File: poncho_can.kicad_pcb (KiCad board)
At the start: 2 copper layers, 85.7 x 79.6 mm, 40 parts, among them J10 GS2, J101 DB9_Male_MountingHoles, J102 DB9_Male_MountingHoles, J103 GS2, J104 GS2, J105 GS2, J106 GS2, J7 GS2, J8 GS2, J9 GS2, U101 TJA1051T, U102 TJA1051T

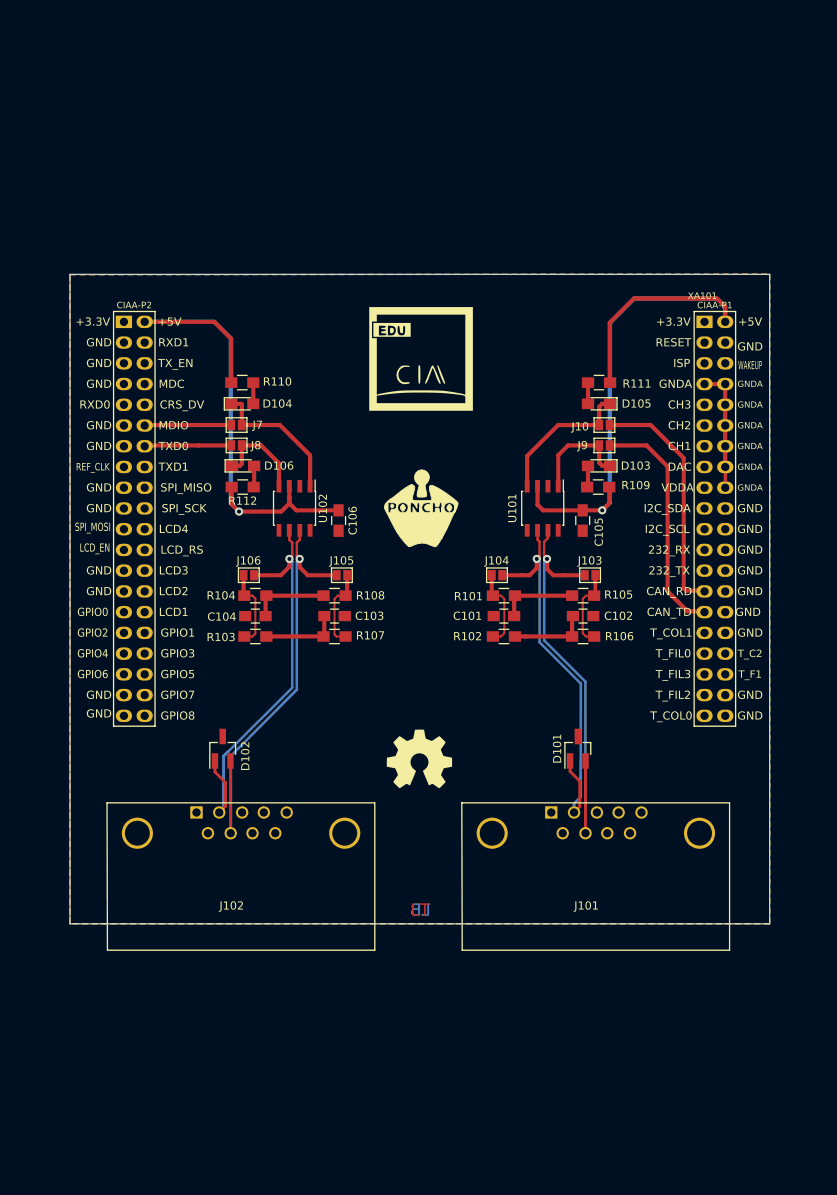
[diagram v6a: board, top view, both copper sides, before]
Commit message: Agrego documentacion y aplica cambios sugeridos en la revision
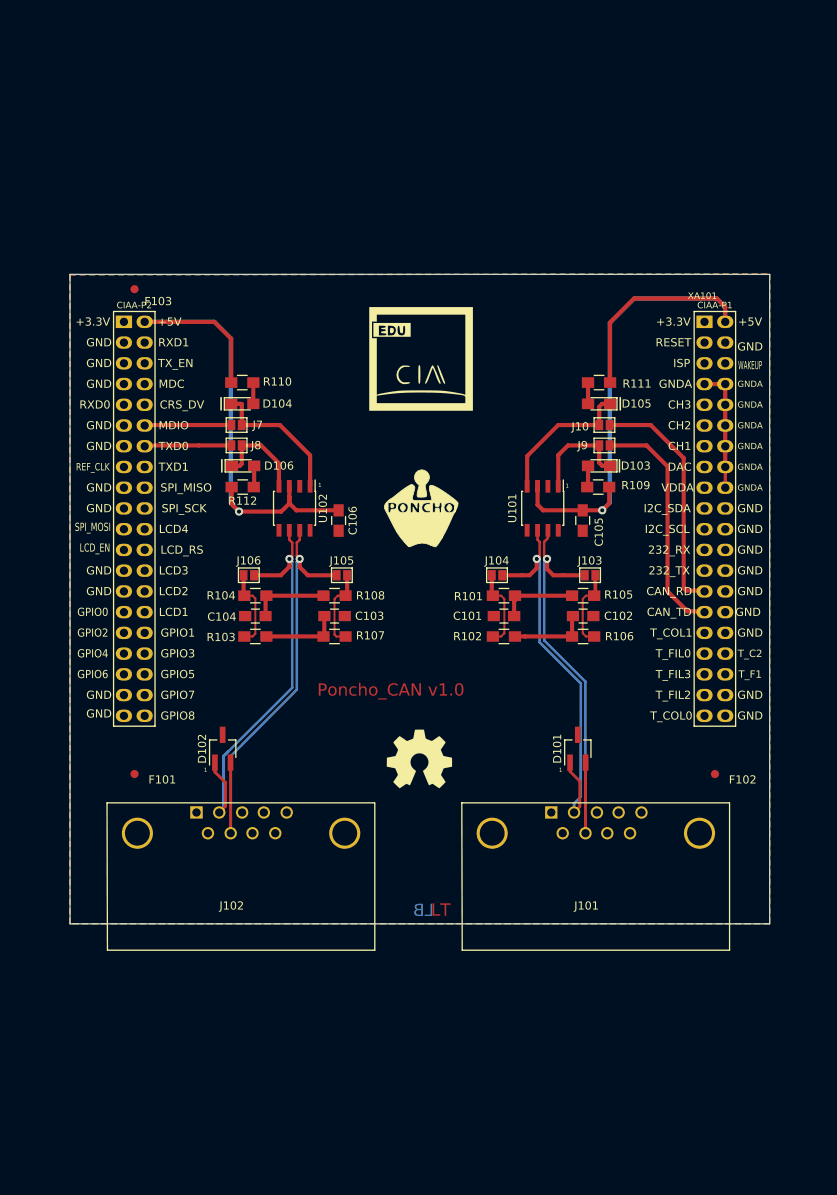
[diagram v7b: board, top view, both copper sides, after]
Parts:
- added F101: Fiduciaria, Fiducials:Fiducial_1mm_Dia_2.54mm_Outer_CopperBottom, F.Cu at (73.7, 115.6)
- added F102: Fiduciaria, Fiducials:Fiducial_1mm_Dia_2.54mm_Outer_CopperBottom, F.Cu at (144.8, 115.6)
- added F103: Fiduciaria, Fiducials:Fiducial_1mm_Dia_2.54mm_Outer_CopperBottom, F.Cu at (73.7, 56.2)
- D101, D102: footprint TO_SOT_Packages_SMD:SOT-23_Handsoldering -> TO_SOT_Packages_SMD:SOT-23W_Handsoldering
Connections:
- J101 pad 1: (no net) -> Net-(J101-Pad1)
- J101 pad 4: (no net) -> Net-(J101-Pad4)
- J101 pad 5: (no net) -> Net-(J101-Pad5)
- J101 pad 6: (no net) -> Net-(J101-Pad6)
- J101 pad 8: (no net) -> Net-(J101-Pad8)
- J101 pad 9: (no net) -> Net-(J101-Pad9)
- J102 pad 1: (no net) -> Net-(J102-Pad1)
- J102 pad 4: (no net) -> Net-(J102-Pad4)
- J102 pad 5: (no net) -> Net-(J102-Pad5)
- J102 pad 6: (no net) -> Net-(J102-Pad6)
- J102 pad 8: (no net) -> Net-(J102-Pad8)
- J102 pad 9: (no net) -> Net-(J102-Pad9)
- U101 pad 5: (no net) -> Net-(U101-Pad5)
- U101 pad 8: (no net) -> Net-(U101-Pad8)
- U102 pad 5: (no net) -> Net-(U102-Pad5)
- U102 pad 8: (no net) -> Net-(U102-Pad8)
- XA101 pad 1: (no net) -> +3V3
- XA101 pad 11: (no net) -> Net-(XA101-Pad11)
- XA101 pad 13: (no net) -> Net-(XA101-Pad13)
- XA101 pad 15: (no net) -> Net-(XA101-Pad15)
- XA101 pad 17: (no net) -> Net-(XA101-Pad17)
- XA101 pad 19: (no net) -> Net-(XA101-Pad19)
- XA101 pad 21: (no net) -> Net-(XA101-Pad21)
- XA101 pad 23: (no net) -> Net-(XA101-Pad23)
- XA101 pad 25: (no net) -> Net-(XA101-Pad25)
- XA101 pad 3: (no net) -> Net-(XA101-Pad3)
- XA101 pad 31: (no net) -> Net-(XA101-Pad31)
- XA101 pad 33: (no net) -> Net-(XA101-Pad33)
- XA101 pad 34: (no net) -> Net-(XA101-Pad34)
- XA101 pad 35: (no net) -> Net-(XA101-Pad35)
- XA101 pad 36: (no net) -> Net-(XA101-Pad36)
- XA101 pad 37: (no net) -> Net-(XA101-Pad37)
- XA101 pad 39: (no net) -> Net-(XA101-Pad39)
- XA101 pad 41: (no net) -> +3.3VP
- XA101 pad 44: (no net) -> Net-(XA101-Pad44)
- XA101 pad 46: (no net) -> Net-(XA101-Pad46)
- XA101 pad 48: (no net) -> Net-(XA101-Pad48)
- XA101 pad 49: (no net) -> Net-(XA101-Pad49)
- XA101 pad 5: (no net) -> Net-(XA101-Pad5)
- XA101 pad 50: (no net) -> Net-(XA101-Pad50)
- XA101 pad 55: (no net) -> Net-(XA101-Pad55)
- XA101 pad 56: (no net) -> Net-(XA101-Pad56)
- XA101 pad 58: (no net) -> Net-(XA101-Pad58)
- XA101 pad 6: (no net) -> Net-(XA101-Pad6)
- XA101 pad 60: (no net) -> Net-(XA101-Pad60)
- XA101 pad 61: (no net) -> Net-(XA101-Pad61)
- XA101 pad 62: (no net) -> Net-(XA101-Pad62)
- XA101 pad 63: (no net) -> Net-(XA101-Pad63)
- XA101 pad 64: (no net) -> Net-(XA101-Pad64)
- XA101 pad 66: (no net) -> Net-(XA101-Pad66)
- XA101 pad 68: (no net) -> Net-(XA101-Pad68)
- XA101 pad 69: (no net) -> Net-(XA101-Pad69)
- XA101 pad 70: (no net) -> Net-(XA101-Pad70)
- XA101 pad 71: (no net) -> Net-(XA101-Pad71)
- XA101 pad 72: (no net) -> Net-(XA101-Pad72)
- XA101 pad 73: (no net) -> Net-(XA101-Pad73)
- XA101 pad 74: (no net) -> Net-(XA101-Pad74)
- XA101 pad 75: (no net) -> Net-(XA101-Pad75)
- XA101 pad 76: (no net) -> Net-(XA101-Pad76)
- XA101 pad 78: (no net) -> Net-(XA101-Pad78)
- XA101 pad 80: (no net) -> Net-(XA101-Pad80)
- XA101 pad 9: (no net) -> Net-(XA101-Pad9)
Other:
- board text added: "1"
- board text added: "Diseño doble faz con componentes en capa superior Sin requerimientos especiales."
- board text added: "Grilla 0.1mm Margen 3mm Vias 1mm - agujero vias 0.5mm Track mas pequeño 0.254mm (10mils)"
- board text added: "Poncho_CAN v1.0"
- board text removed: "Diseño simple faz. Sin requerimientos especiales."
- board text removed: "Editar el rótulo"
- board text removed: "Editar este cuadro para reflejar cantidad de capas, si se han realizado cálculos de impedancia o si es relevante para el funcionamiento."

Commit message: Rehago el fill de cobre para que quede bien indicado en la placa. Edito las comentarios en el pcb con el valor del clearence corregido
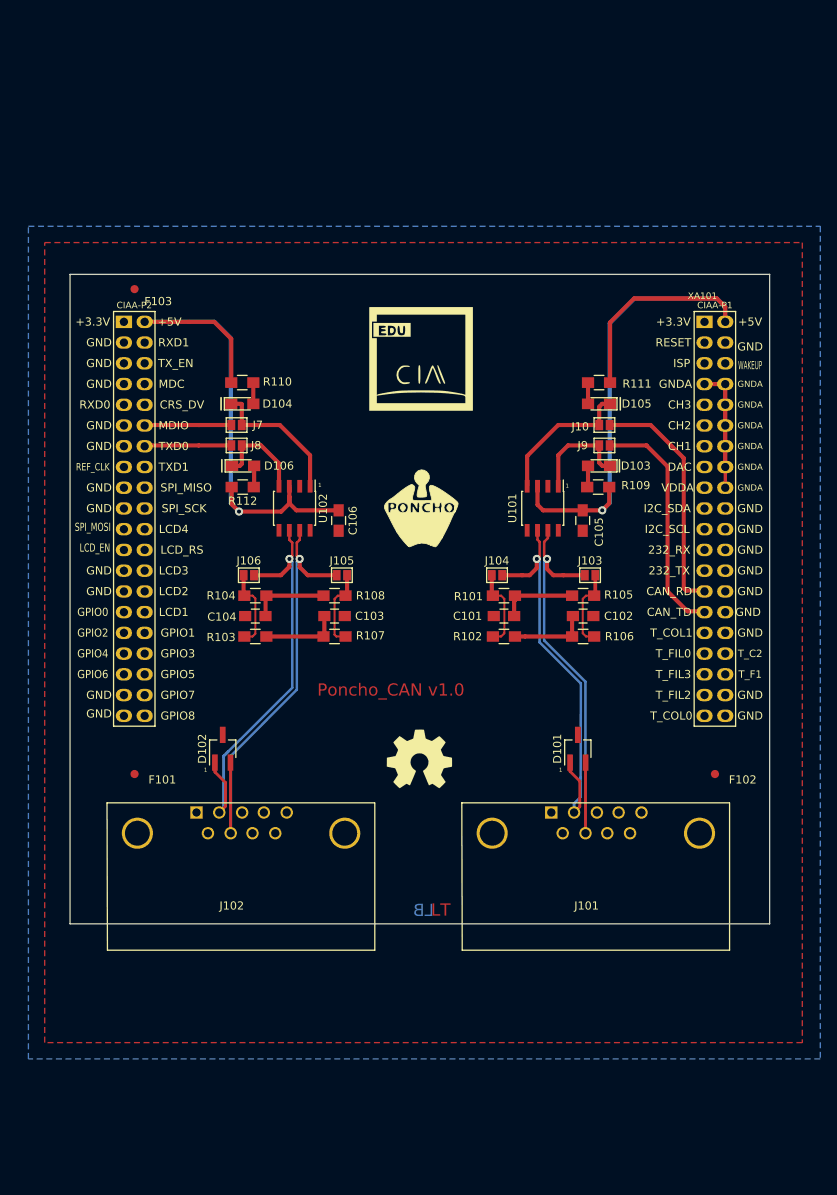
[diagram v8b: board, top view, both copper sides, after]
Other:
- net class Default: clearance 0.1524 -> 0.25
- rule trace_clearance: 0.1524 -> 0.25
- board text added: "Grilla 0.1mm Clearence 0.25mm Vias 1mm - agujero vias 0.5mm Track mas pequeño 0.254mm (10mils)"
- board text removed: "Grilla 0.1mm Margen 3mm Vias 1mm - agujero vias 0.5mm Track mas pequeño 0.254mm (10mils)"
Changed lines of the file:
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@@
   (general
     (links 90)
-    (no_connects 0)
-    (area 65.724999 54.319999 151.575001 134.025001)
+    (no_connects 32)
+    (area 17.572141 15.774999 279.500001 146.235001)
     (thickness 1.6)
-    (drawings 29)
+    (drawings 27)
     (tracks 206)
     (zones 0)
@@
     (user_trace_width 0.3556)
     (user_trace_width 0.508)
-    (trace_clearance 0.1524)
+    (trace_clearance 0.25)
     (zone_clearance 0.2032)
     (zone_45_only no)
@@
   (net 90 "Net-(XA101-Pad80)")
   (net_class Default "This is the default net class."
-    (clearance 0.1524)
+    (clearance 0.25)
     (trace_width 0.1524)
     (via_dia 1)
@@
     (effects (font (size 1.5 1.5) (thickness 0.3)))
   )
-  (gr_text "Grilla 0.1mm\nMargen 3mm\nVias 1mm - agujero vias 0.5mm\nTrack mas pequeño 0.254mm (10mils)" (at 18.2 58.7) (layer Dwgs.User)
+  (gr_text "Grilla 0.1mm\nClearence 0.25mm\nVias 1mm - agujero vias 0.5mm\nTrack mas pequeño 0.254mm (10mils)" (at 19 37.8) (layer Dwgs.User)
     (effects (font (size 1.5 1.5) (thickness 0.3)) (justify left))
-  )
-  (dimension 85.7 (width 0.3) (layer Dwgs.User)
-    (gr_text "85,700 mm" (at 108.65 49.35) (layer Dwgs.User)
-      (effects (font (size 1.5 1.5) (thickness 0.3)))
-    )
-    (feature1 (pts (xy 151.5 54.4) (xy 151.5 48)))
-    (feature2 (pts (xy 65.8 54.4) (xy 65.8 48)))
-    (crossbar (pts (xy 65.8 50.7) (xy 151.5 50.7)))
-    (arrow1a (pts (xy 151.5 50.7) (xy 150.373496 51.286421)))
-    (arrow1b (pts (xy 151.5 50.7) (xy 150.373496 50.113579)))
-    (arrow2a (pts (xy 65.8 50.7) (xy 66.926504 51.286421)))
-    (arrow2b (pts (xy 65.8 50.7) (xy 66.926504 50.113579)))
-  )
-  (dimension 79.6 (width 0.3) (layer Dwgs.User)
-    (gr_text "79,600 mm" (at 162.15 94.2 270) (layer Dwgs.User)
-      (effects (font (size 1.5 1.5) (thickness 0.3)))
-    )
-    (feature1 (pts (xy 151.5 134) (xy 163.5 134)))
-    (feature2 (pts (xy 151.5 54.4) (xy 163.5 54.4)))
-    (crossbar (pts (xy 160.8 54.4) (xy 160.8 134)))
-    (arrow1a (pts (xy 160.8 134) (xy 160.213579 132.873496)))
-    (arrow1b (pts (xy 160.8 134) (xy 161.386421 132.873496)))
-    (arrow2a (pts (xy 160.8 54.4) (xy 160.213579 55.526504)))
-    (arrow2b (pts (xy 160.8 54.4) (xy 161.386421 55.526504)))
   )
   (gr_text "    LB" (at 110.4 132.3) (layer B.Cu)
@@
     (polygon
       (pts
-        (xy 65.8 54.45) (xy 151.5 54.35) (xy 151.5 133.95) (xy 65.8 133.95)
+        (xy 155.5 50.5) (xy 155.5 148.5) (xy 62.7 148.5) (xy 62.7 50.5)
       )
     )
@@
     (polygon
       (pts
-        (xy 65.8 54.45) (xy 151.5 54.35) (xy 151.5 133.95) (xy 65.8 133.95) (xy 65.8 54.35)
+        (xy 157.7 48.5) (xy 157.7 150.5) (xy 60.7 150.5) (xy 60.7 48.5)
       )
     )
